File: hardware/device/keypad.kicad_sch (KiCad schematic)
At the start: 76 parts, among them SW1 TRIG1, SW10 TRIG10, SW11 TRIG11, SW12 TRIG12, SW13 TRIG13, SW14 TRIG14, SW15 TRIG15, SW16 TRIG16, SW17 WHEEL_BTN, SW18 HELP, SW19 LEFT_BTN, SW2 TRIG2, SW20 RIGHT_BTN, SW3 TRIG3, SW4 TRIG4, SW5 TRIG5, SW6 TRIG6, SW7 TRIG7, SW8 TRIG8, SW9 TRIG9, U25 TCA8418RTWR

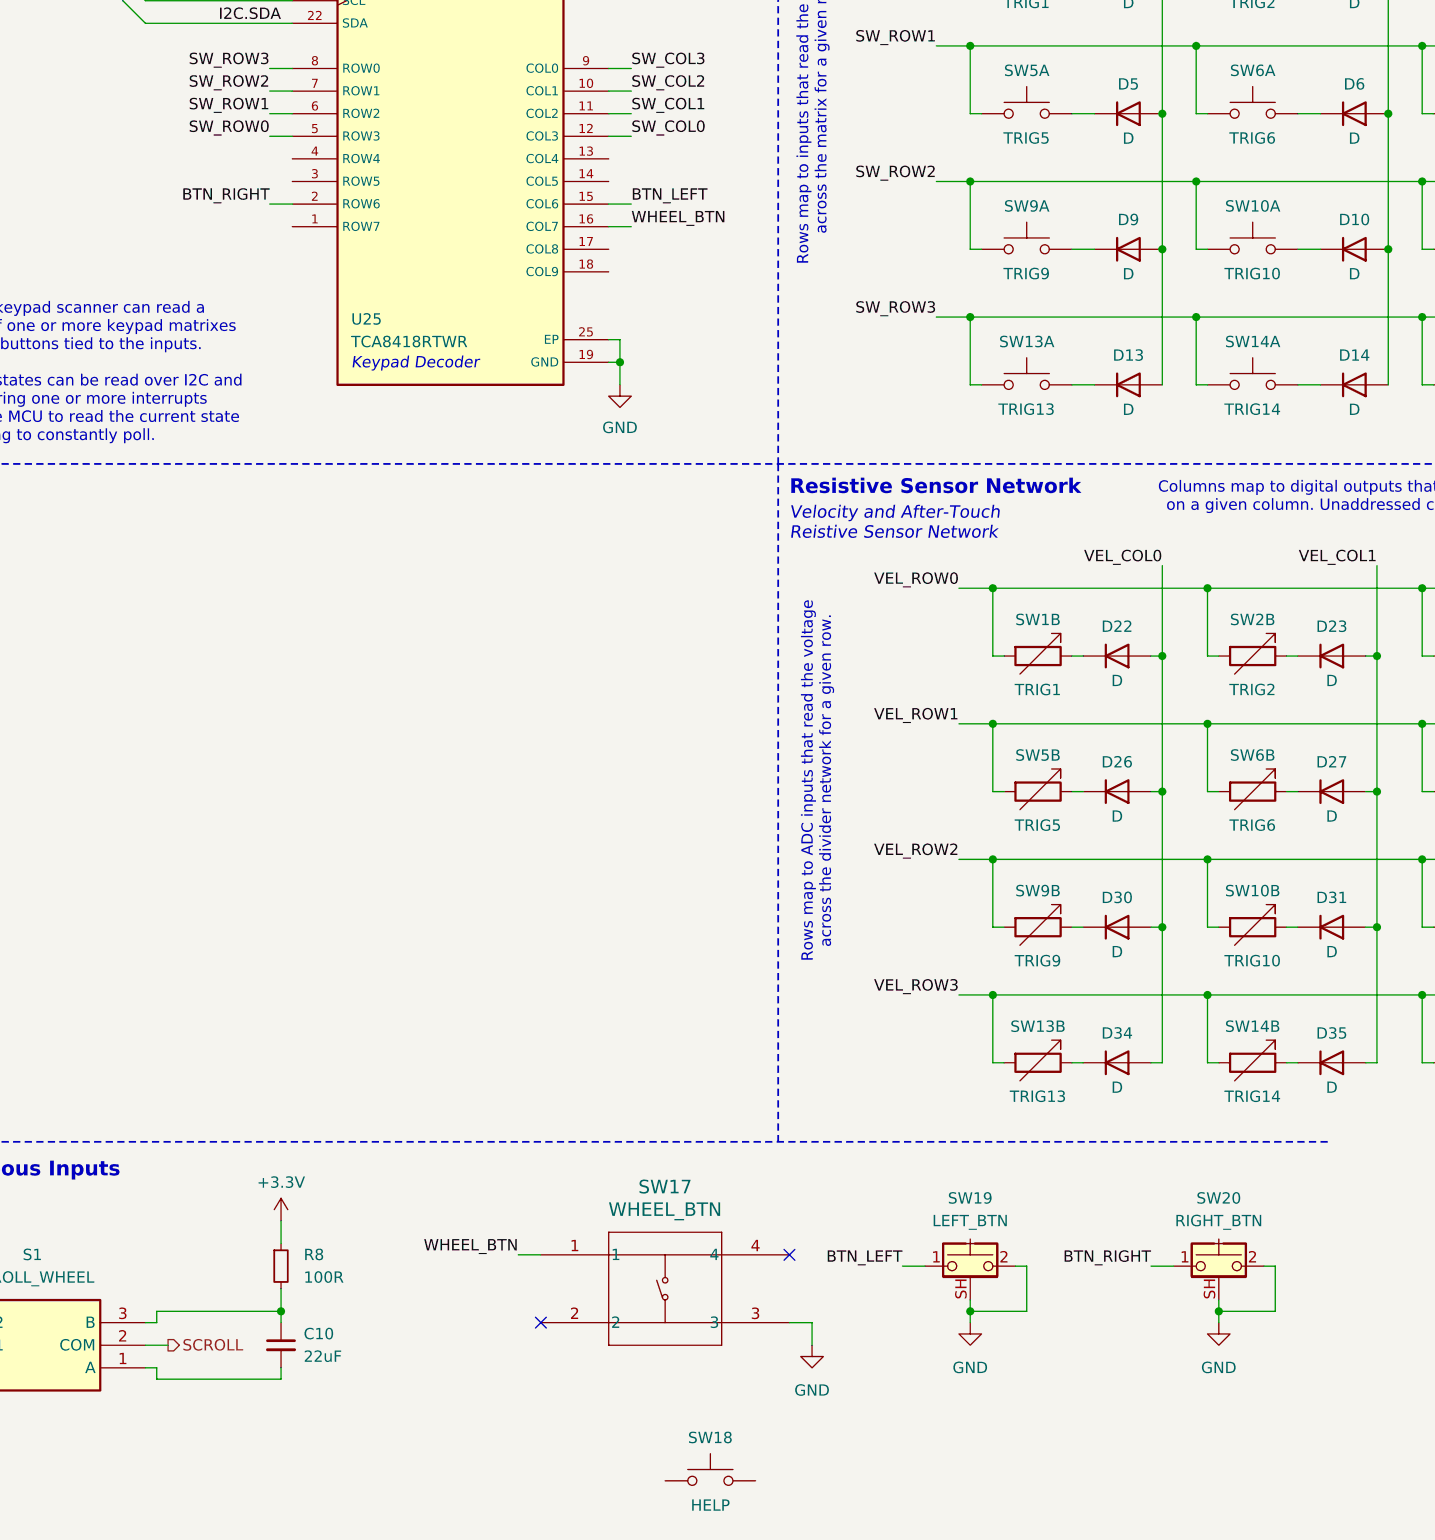
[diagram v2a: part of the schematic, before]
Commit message: feat: various routing, footprint and schematic cleanup
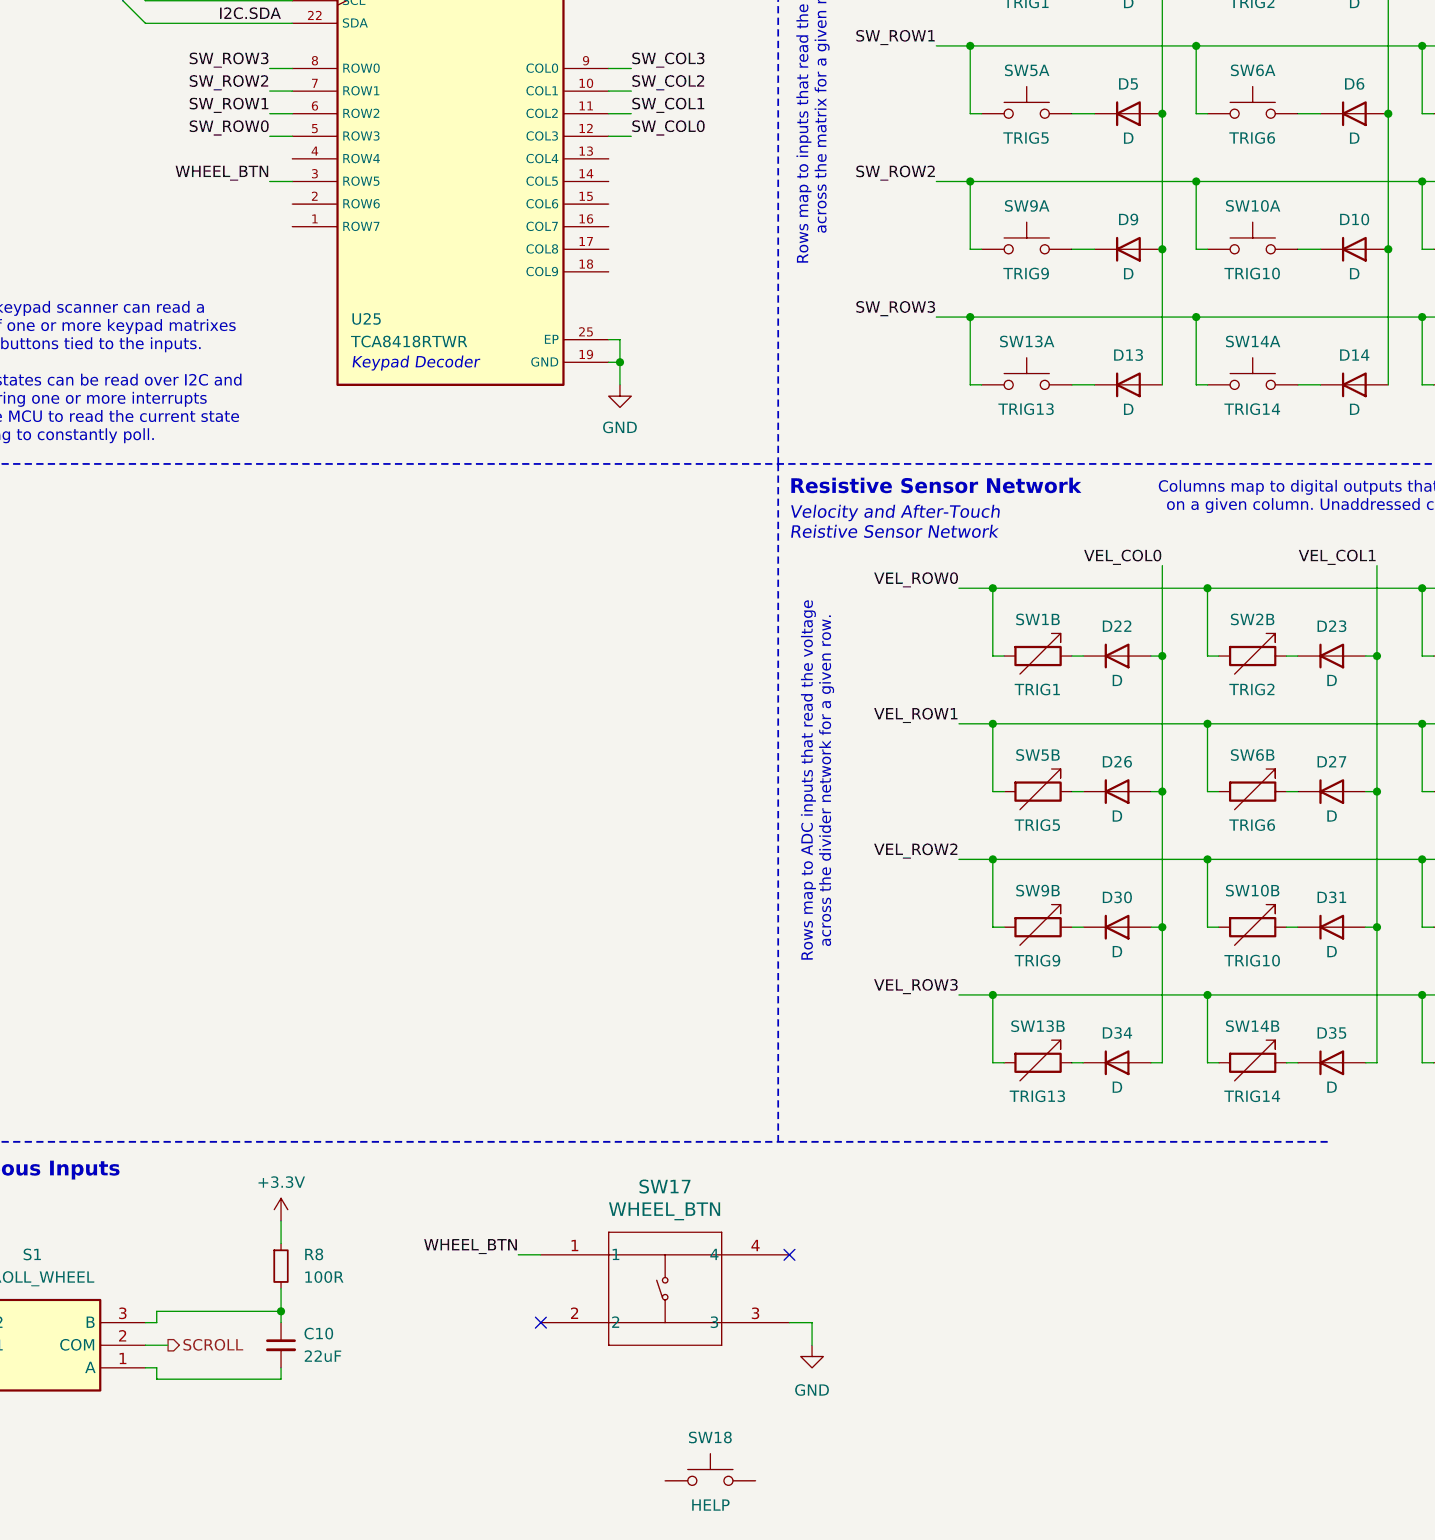
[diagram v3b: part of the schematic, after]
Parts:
- removed SW19: LEFT_BTN, Button_Switch_SMD:SW_Push_1P1T-MP_NO_Horizontal_Alps_SKRTLAE010, symbol Switch:SW_Push_Shielded
- removed SW20: RIGHT_BTN, Button_Switch_SMD:SW_Push_1P1T-MP_NO_Horizontal_Alps_SKRTLAE010, symbol Switch:SW_Push_Shielded
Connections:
- net WHEEL_BTN: now also U25.3 (ROW5); no longer U25.16 (COL7)
- net BTN_LEFT: no longer names the net of U25.15 (COL6)
- net BTN_RIGHT: no longer names the net of U25.2 (ROW6)

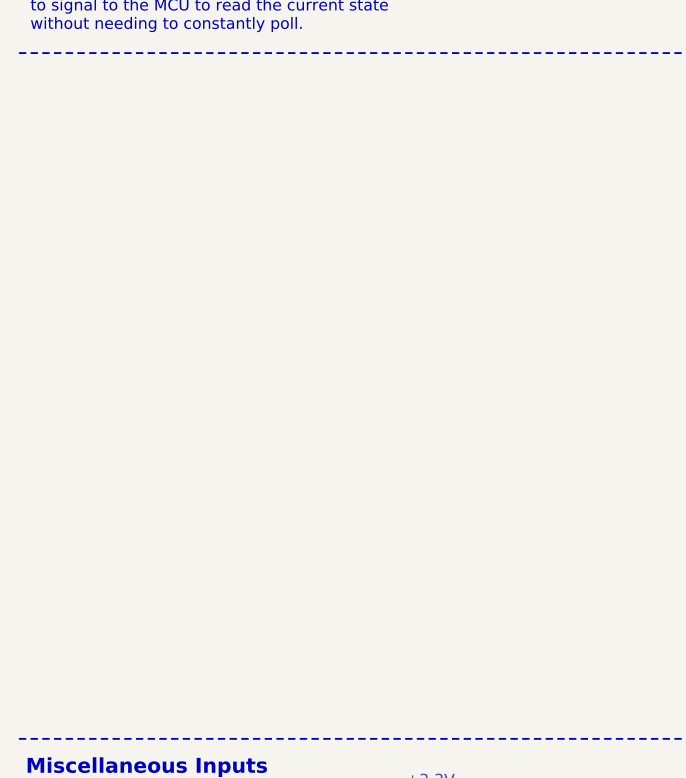
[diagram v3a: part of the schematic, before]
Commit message: feat: add SWD connector, route bluetooth, route velocity matrix
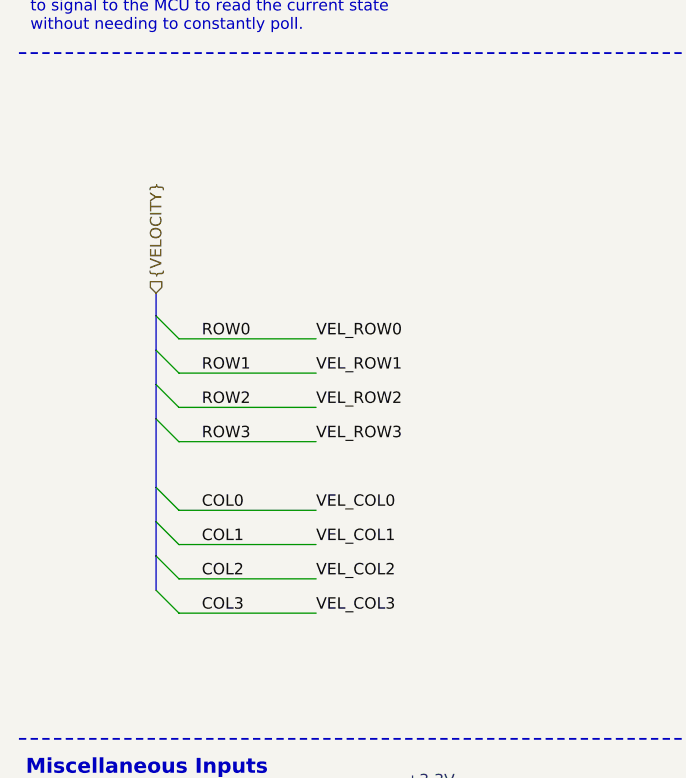
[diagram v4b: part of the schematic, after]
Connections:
- net VEL_COL0 renamed COL0
- net VEL_COL1 renamed COL1
- net VEL_COL2 renamed COL2
- net VEL_COL3 renamed COL3
- net VEL_ROW0 renamed ROW0
- net VEL_ROW1 renamed ROW1
- net VEL_ROW2 renamed ROW2
- net VEL_ROW3 renamed ROW3
